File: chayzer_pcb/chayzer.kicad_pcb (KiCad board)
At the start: 2 copper layers, 134 x 81 mm, 30 parts, among them U1 ProMicro

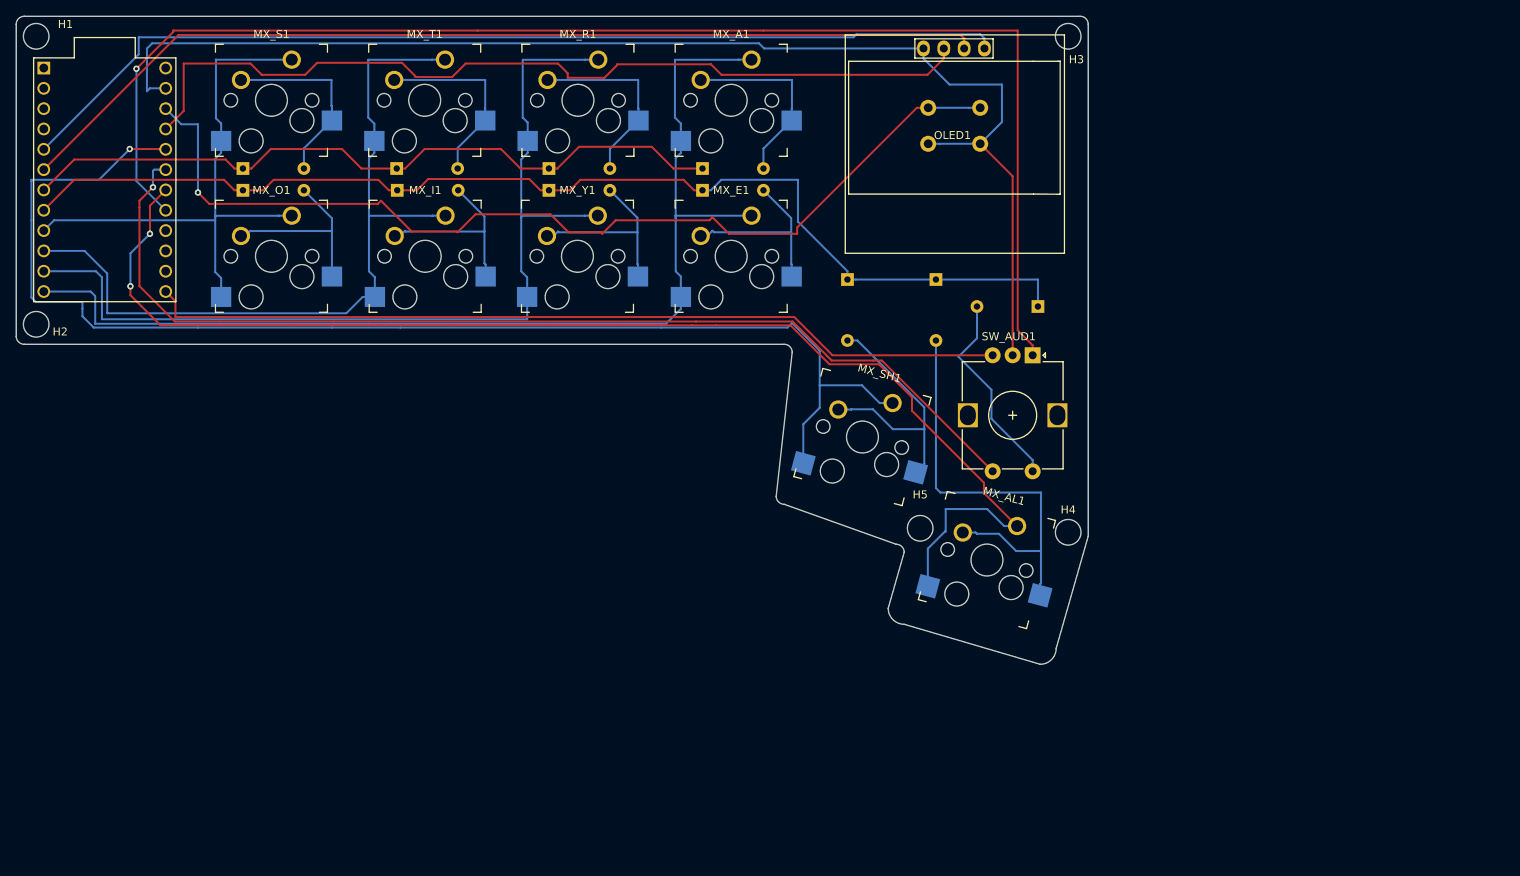
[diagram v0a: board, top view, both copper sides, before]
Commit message: moved the encoder up a bit
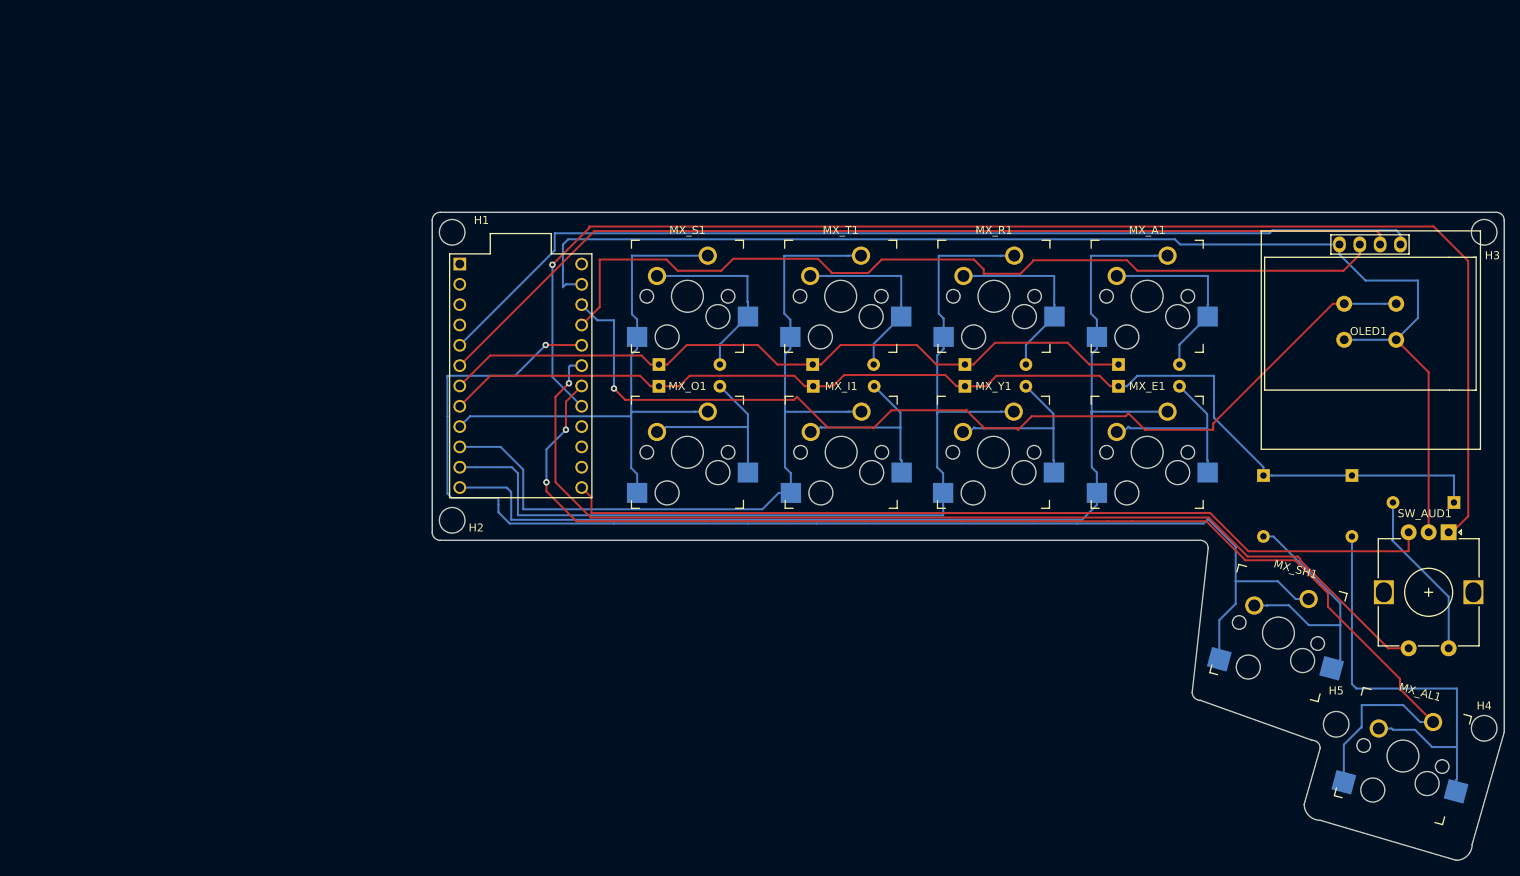
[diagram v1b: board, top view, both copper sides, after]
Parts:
- moved D_A1 57.5 mm to (168.8, 85.5)
- moved D_AL1 57.5 mm to (198.0, 99.4)
- moved D_AUD1 57.5 mm to (210.7, 102.8)
- moved D_E1 57.5 mm to (168.8, 88.2)
- moved D_I1 57.5 mm to (130.6, 88.2)
- moved D_O1 57.5 mm to (111.3, 88.2)
- moved D_R1 57.5 mm to (149.6, 85.5)
- moved D_S1 57.5 mm to (111.3, 85.5)
- moved D_SH1 57.5 mm to (186.9, 99.4)
- moved D_T1 57.5 mm to (130.6, 85.5)
- moved D_Y1 57.5 mm to (149.6, 88.2)
- moved H1 57.5 mm to (85.5, 69.0)
- moved H2 57.5 mm to (85.5, 105.0)
- moved H3 57.5 mm to (214.5, 69.0)
- moved H4 57.5 mm to (214.5, 131.0)
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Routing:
- net Net-(D_AUD1-Pad2): track 25.4 -> 21.2 mm
- net Net-(SW_AUD1-PadB): track 107.8 -> 110.2 mm
- net GND: track 161.0 -> 158.6 mm
- net Net-(SW_AUD1-PadS2): track 133.0 -> 132.1 mm

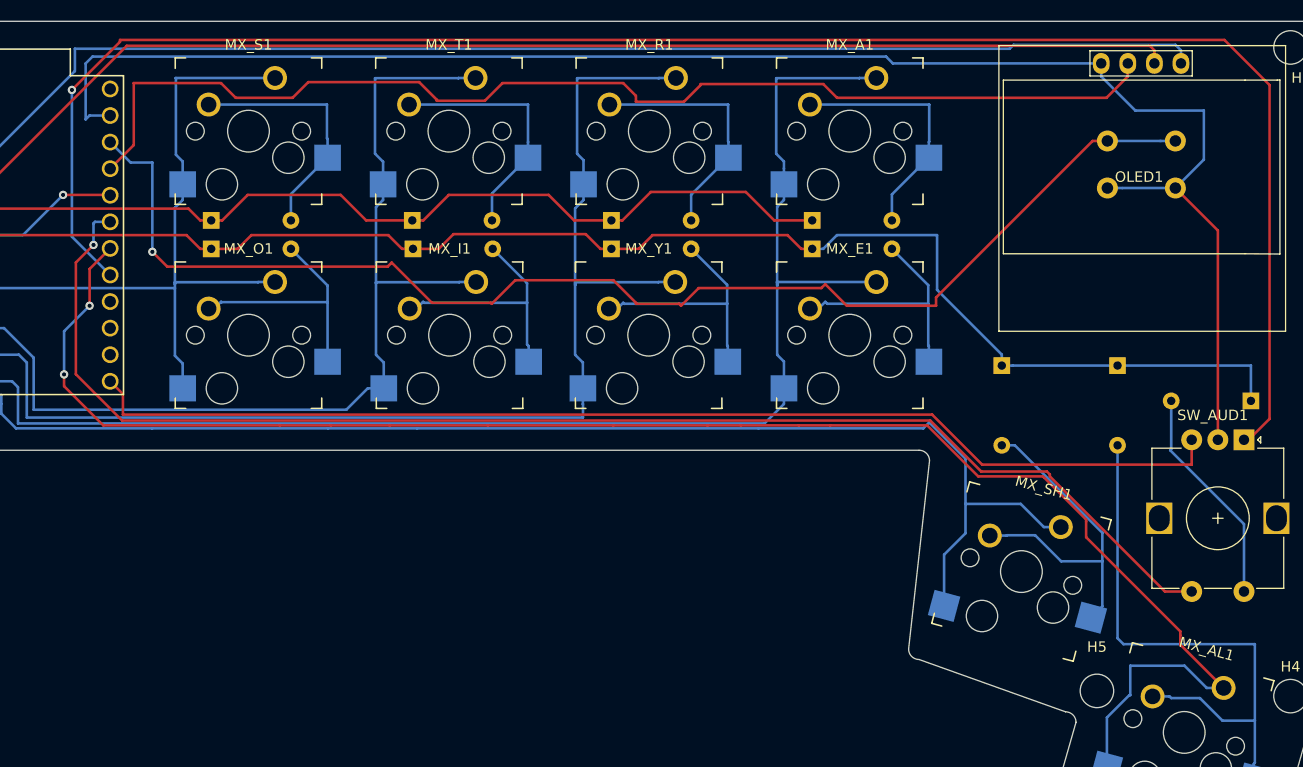
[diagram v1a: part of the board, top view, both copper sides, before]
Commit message: added rgb to PCB, buggy in qmk right now, and untested on PCB
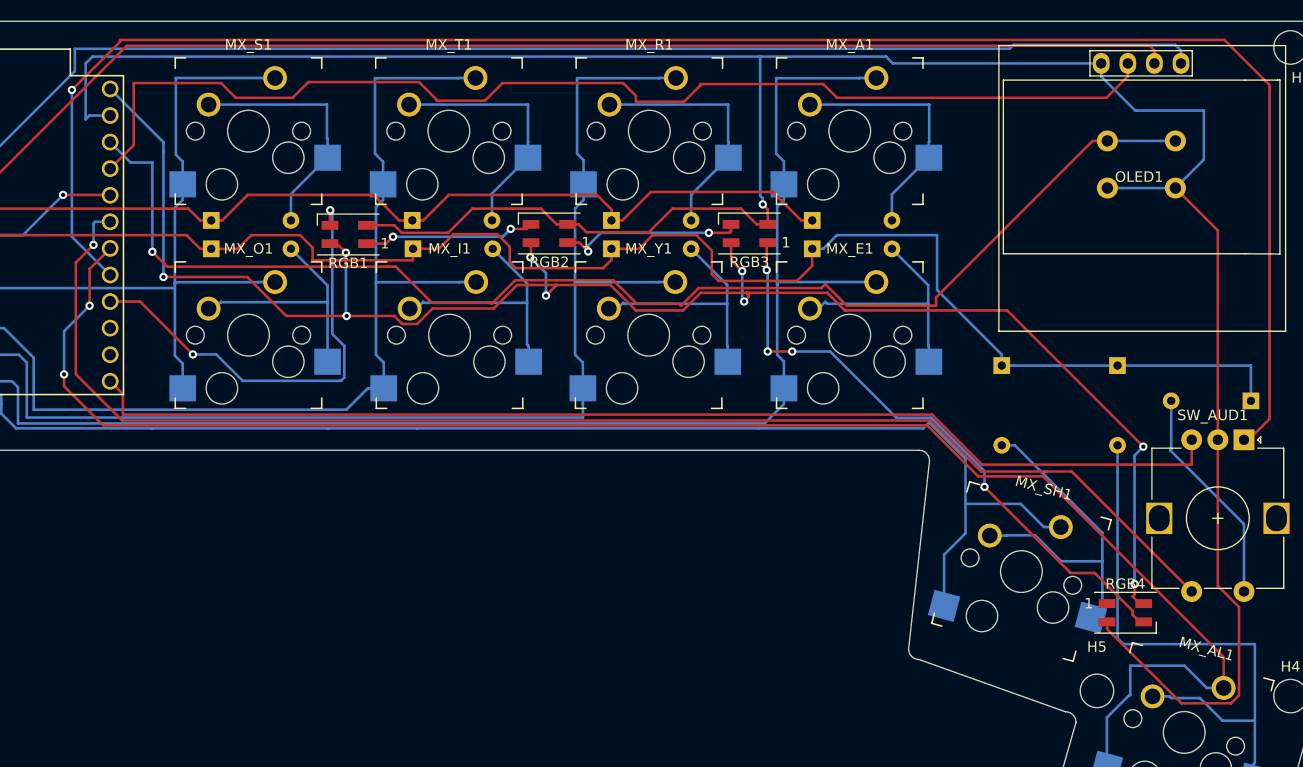
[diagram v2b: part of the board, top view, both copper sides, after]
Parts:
- added RGB1: SK6812MINI, LED_SMD:LED_SK6812MINI_PLCC4_3.5x3.5mm_P1.75mm, F.Cu at (124.4, 86.9)
- added RGB2: SK6812MINI, LED_SMD:LED_SK6812MINI_PLCC4_3.5x3.5mm_P1.75mm, F.Cu at (143.7, 86.8)
- added RGB3: SK6812MINI, LED_SMD:LED_SK6812MINI_PLCC4_3.5x3.5mm_P1.75mm, F.Cu at (162.8, 86.8)
- added RGB4: SK6812MINI, LED_SMD:LED_SK6812MINI_PLCC4_3.5x3.5mm_P1.75mm, F.Cu at (198.7, 123.0)
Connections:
- net Net-(D_A1-Pad1) renamed D4
- net Net-(D_AL1-Pad1) renamed C6
- net Net-(MX_A1-Pad1) renamed B5
- net Net-(MX_AL1-Pad1) renamed F6
- net Net-(MX_I1-Pad1) renamed E6
- net Net-(MX_O1-Pad1) renamed D7
- net Net-(MX_R1-Pad1) renamed B4
- net Net-(MX_SH1-Pad1) renamed F4
- net Net-(OLED1-Pad2) renamed VCC
- net Net-(OLED1-Pad3) renamed SCL
- net Net-(OLED1-Pad4) renamed SDA
- net Net-(SW_AUD1-PadA) renamed F7
- net Net-(SW_AUD1-PadB) renamed B6
- net Net-(SW_AUD1-PadS2) renamed F5
- net Net-(SW_RES1-Pad2) renamed RST
- U1 pad 16: Net-(U1-Pad16) -> B1
- U1 pad 24: +5V -> 5v
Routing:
- net 5v: track 0.00 -> 163.4 mm, vias 0 -> 9
- net GND: track 158.6 -> 258.9 mm, vias 0 -> 1
- net Net-(RGB3-Pad1): track 0.00 -> 58.2 mm, vias 0 -> 4
- net B1: track 0.00 -> 43.6 mm, vias 0 -> 2
- net Net-(RGB2-Pad1): track 0.00 -> 17.8 mm, vias 0 -> 2
- net Net-(RGB1-Pad1): track 0.00 -> 16.5 mm, vias 0 -> 2
- net C6: track 142.5 -> 152.6 mm
- net D4: track 90.7 -> 91.3 mm
